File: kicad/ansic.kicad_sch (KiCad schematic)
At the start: 56 parts, among them J1 AudioJack4, J2 AudioJack4, J3 Conn_01x02_Socket, SW1 SW_Push, SW10 SW_Push, SW11 SW_Push, SW12 SW_Push, SW13 SW_Push, SW14 SW_Push, SW15 SW_Push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

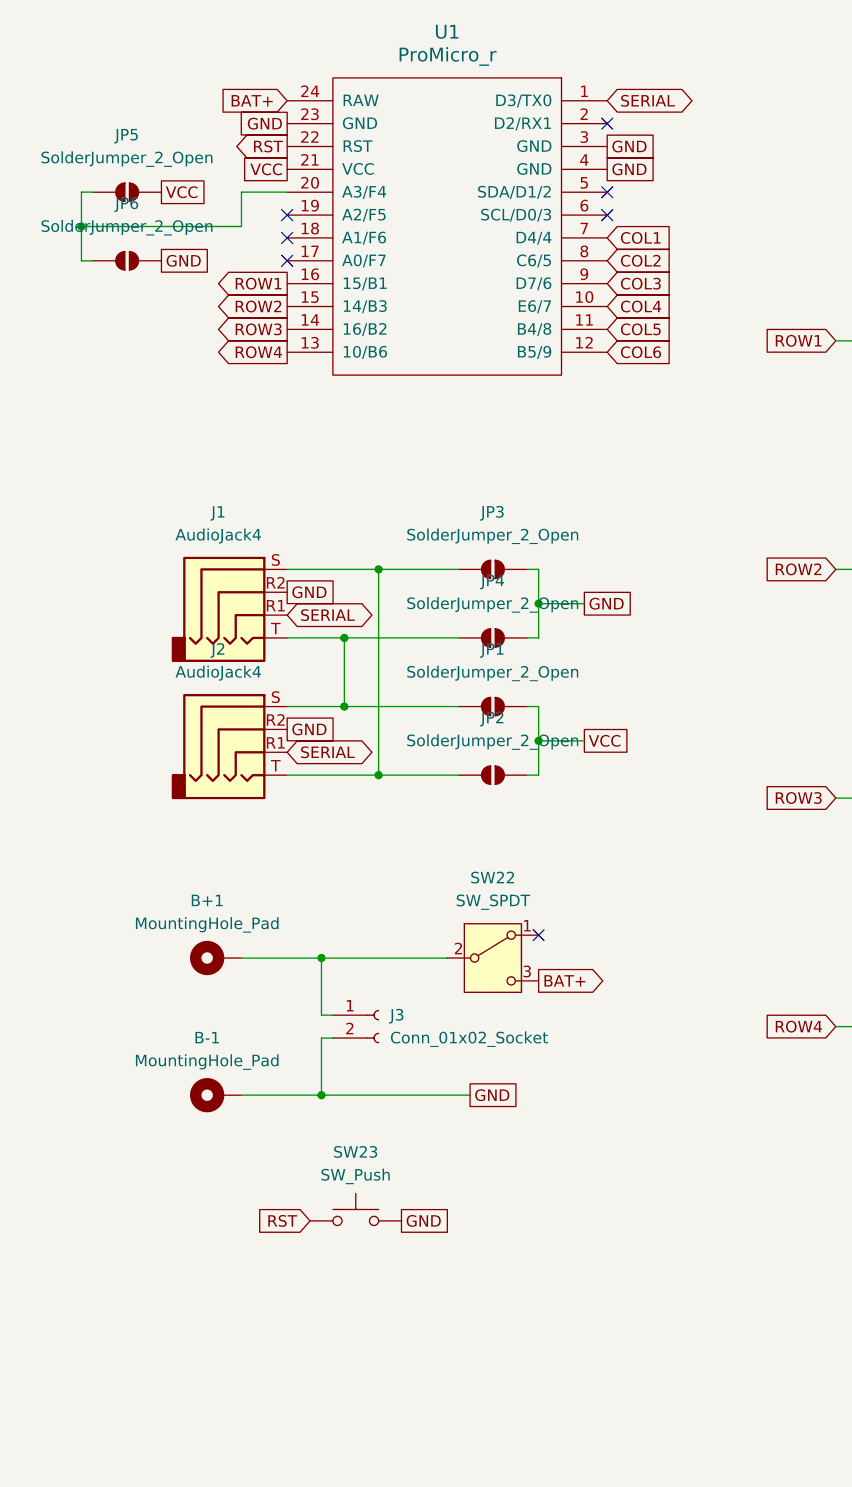
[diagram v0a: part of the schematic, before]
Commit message: edit for more readable schema
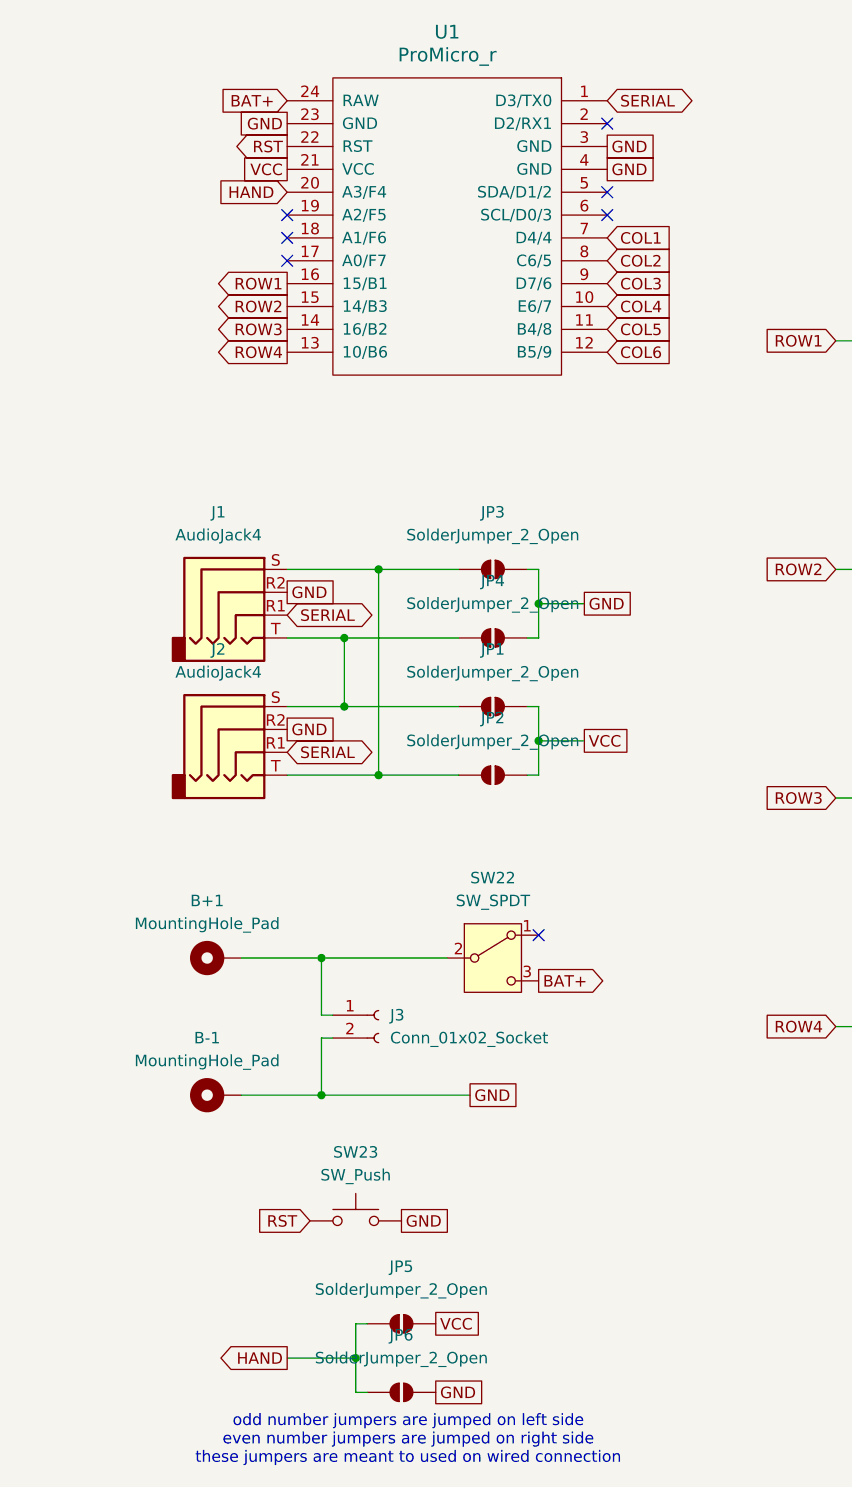
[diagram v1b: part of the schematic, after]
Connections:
- net HAND: now reaches JP5.2 (B), JP6.2 (B), U1.20 (A3/F4)
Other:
- note added: "odd number jumpers are jumped on left side even number jumpers are jumped on right side these jumpers are meant to used on wired connection"
- moved on the sheet: JP5, JP6
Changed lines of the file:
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@@
 	(generator_version "9.0")
 	(paper "A4")
+	(text "odd number jumpers are jumped on left side\neven number jumpers are jumped on right side\nthese jumpers are meant to used on wired connection"
+		(exclude_from_sim no)
+		(at 54.102 172.974 0)
+		(effects
+			(font
+				(size 1.27 1.27)
+			)
+		)
+	)
 	(junction
 		(at 165.1 50.8)
@@
 	)
 	(junction
-		(at 114.3 127)
+		(at 48.26 163.83)
 		(diameter 0)
 		(color 0 0 0 0)
 	)
 	(junction
-		(at 228.6 88.9)
+		(at 114.3 127)
 		(diameter 0)
 		(color 0 0 0 0)
 	)
 	(junction
-		(at 17.78 38.1)
+		(at 228.6 88.9)
 		(diameter 0)
 		(color 0 0 0 0)
@@
 	(wire
 		(pts
+			(xy 40.64 163.83) (xy 48.26 163.83)
+		)
+		(stroke
+			(width 0)
+			(type default)
+		)
+	)
+	(wire
+		(pts
 			(xy 44.45 134.62) (xy 35.56 134.62)
 		)
@@
 	(wire
 		(pts
-			(xy 114.3 99.06) (xy 114.3 101.6)
+			(xy 48.26 163.83) (xy 48.26 167.64)
 		)
 		(stroke
@@
 	(wire
 		(pts
-			(xy 203.2 38.1) (xy 203.2 63.5)
+			(xy 114.3 99.06) (xy 114.3 101.6)
 		)
 		(stroke
@@
 	(wire
 		(pts
-			(xy 35.56 34.29) (xy 35.56 38.1)
+			(xy 203.2 38.1) (xy 203.2 63.5)
 		)
 		(stroke
@@
 	(wire
 		(pts
-			(xy 35.56 38.1) (xy 17.78 38.1)
-		)
-		(stroke
-			(width 0)
-			(type default)
-		)
-	)
-	(wire
-		(pts
 			(xy 139.7 50.8) (xy 165.1 50.8)
 		)
@@
 	(wire
 		(pts
-			(xy 17.78 41.91) (xy 19.05 41.91)
+			(xy 48.26 167.64) (xy 49.53 167.64)
 		)
 		(stroke
@@
 	(wire
 		(pts
-			(xy 19.05 34.29) (xy 17.78 34.29)
+			(xy 49.53 160.02) (xy 48.26 160.02)
 		)
 		(stroke
@@
 	(wire
 		(pts
-			(xy 17.78 34.29) (xy 17.78 38.1)
-		)
-		(stroke
-			(width 0)
-			(type default)
-		)
-	)
-	(wire
-		(pts
 			(xy 139.7 38.1) (xy 139.7 40.64)
 		)
@@
 	(wire
 		(pts
-			(xy 17.78 38.1) (xy 17.78 41.91)
+			(xy 48.26 160.02) (xy 48.26 163.83)
 		)
 		(stroke
@@
 	(wire
 		(pts
-			(xy 40.64 34.29) (xy 35.56 34.29)
-		)
-		(stroke
-			(width 0)
-			(type default)
-		)
-	)
-	(wire
-		(pts
 			(xy 252.73 88.9) (xy 254 88.9)
 		)
@@
 		)
 	)
+	(global_label "HAND"
+		(shape input)
+		(at 40.64 34.29 180)
+		(fields_autoplaced yes)
+		(effects
+			(font
+				(size 1.27 1.27)
+			)
+			(justify right)
+		)
+		(property "Intersheetrefs" "${INTERSHEET_REFS}"
+			(at 32.6352 34.29 0)
+			(effects
+				(font
+					(size 1.27 1.27)
+				)
+				(justify right)
+				(hide yes)
+			)
+		)
+	)
 	(global_label "GND"
 		(shape passive)
@@
 	(global_label "VCC"
 		(shape passive)
-		(at 26.67 34.29 0)
+		(at 57.15 160.02 0)
 		(fields_autoplaced yes)
 		(effects
@@
 		)
 		(property "Intersheetrefs" "${INTERSHEET_REFS}"
-			(at 32.8 34.29 0)
+			(at 63.28 160.02 0)
 			(effects
 				(font
@@
 		)
 	)
+	(global_label "HAND"
+		(shape output)
+		(at 40.64 163.83 180)
+		(fields_autoplaced yes)
+		(effects
+			(font
+				(size 1.27 1.27)
+			)
+			(justify right)
+		)
+		(property "Intersheetrefs" "${INTERSHEET_REFS}"
+			(at 32.6352 163.83 0)
+			(effects
+				(font
+					(size 1.27 1.27)
+				)
+				(justify right)
+				(hide yes)
+			)
+		)
+	)
 	(global_label "SERIAL"
 		(shape bidirectional)
@@
 	(global_label "GND"
 		(shape passive)
-		(at 26.67 41.91 0)
+		(at 57.15 167.64 0)
 		(fields_autoplaced yes)
 		(effects
@@
 		)
 		(property "Intersheetrefs" "${INTERSHEET_REFS}"
-			(at 33.5257 41.91 0)
+			(at 64.0057 167.64 0)
 			(effects
 				(font
@@
 	(symbol
 		(lib_id "Jumper:SolderJumper_2_Open")
-		(at 22.86 41.91 0)
+		(at 53.34 167.64 0)
 		(mirror y)
 		(unit 1)
@@
 		(fields_autoplaced yes)
 		(property "Reference" "JP6"
-			(at 22.86 35.56 0)
+			(at 53.34 161.29 0)
 			(effects
 				(font
@@
 		)
 		(property "Value" "SolderJumper_2_Open"
-			(at 22.86 38.1 0)
+			(at 53.34 163.83 0)
 			(effects
 				(font
@@
 		)
 		(property "Footprint" ""
-			(at 22.86 41.91 0)
+			(at 53.34 167.64 0)
 			(effects
 				(font
@@
 		)
 		(property "Datasheet" "~"
-			(at 22.86 41.91 0)
+			(at 53.34 167.64 0)
 			(effects
 				(font
@@
 		)
 		(property "Description" "Solder Jumper, 2-pole, open"
-			(at 22.86 41.91 0)
+			(at 53.34 167.64 0)
 			(effects
 				(font
@@
 	(symbol
 		(lib_id "Jumper:SolderJumper_2_Open")
-		(at 22.86 34.29 0)
+		(at 53.34 160.02 0)
 		(mirror y)
 		(unit 1)
@@
 		(fields_autoplaced yes)
 		(property "Reference" "JP5"
-			(at 22.86 27.94 0)
+			(at 53.34 153.67 0)
 			(effects
 				(font
@@
 		)
 		(property "Value" "SolderJumper_2_Open"
-			(at 22.86 30.48 0)
+			(at 53.34 156.21 0)
 			(effects
 				(font
@@
 		)
 		(property "Footprint" ""
-			(at 22.86 34.29 0)
+			(at 53.34 160.02 0)
 			(effects
 				(font
@@
 		)
 		(property "Datasheet" "~"
-			(at 22.86 34.29 0)
+			(at 53.34 160.02 0)
 			(effects
 				(font
@@
 		)
 		(property "Description" "Solder Jumper, 2-pole, open"
-			(at 22.86 34.29 0)
+			(at 53.34 160.02 0)
 			(effects
 				(font
